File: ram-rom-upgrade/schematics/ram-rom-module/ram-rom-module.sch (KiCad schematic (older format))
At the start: 15 parts, among them SW1 SW_DIP_x08, SW2 SW_Push, U1 74LS245, U2 UM61512A, U3 74LS157, U4 28C256, U5 74LS157, U6 74LS157, U7 74LS00

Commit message: first draft of complete design
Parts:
- BAR1: symbol ram-rom-module-parts:BarGraphLED_8P -> ram-rom-upgrade-symbols:BarGraphLED_8P
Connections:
- net BUS_0: now also U1.18 (B0); no longer U1.11 (B7)
- net BUS_1: now also U1.17 (B1); no longer U1.12 (B6)
- net BUS_2: now also U1.16 (B2); no longer U1.13 (B5)
- net BUS_3: now also U1.15 (B3); no longer U1.14 (B4)
- net BUS_4: now also U1.14 (B4); no longer U1.15 (B3)
- net BUS_5: now also U1.13 (B5); no longer U1.16 (B2)
- net BUS_6: now also U1.12 (B6); no longer U1.17 (B1)
- net BUS_7: now also U1.11 (B7); no longer U1.18 (B0)
- net at BAR1.8 (A), U2.13 (I/O1), U3.4 (Za)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: now also U1.2 (A0); no longer U1.9 (A7)
- net at BAR1.7 (A), U2.14 (I/O2), U3.7 (Zb)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: now also U1.3 (A1); no longer U1.8 (A6)
- net at BAR1.6 (A), U2.15 (I/O3), U3.9 (Zc)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: now also U1.4 (A2); no longer U1.7 (A5)
- net at BAR1.5 (A), U2.17 (I/O4), U3.12 (Zd)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: now also U1.5 (A3); no longer U1.6 (A4)
- net at BAR1.4 (A), U2.18 (I/05), U4.16 (D4)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: now also U1.6 (A4); no longer U1.5 (A3)
- net at BAR1.3 (A), U2.19 (I/O6), U4.17 (D5)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: now also U1.7 (A5); no longer U1.4 (A2)
- net at BAR1.2 (A), U2.20 (I/O7), U4.18 (D6)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: now also U1.8 (A6); no longer U1.3 (A1)
- net at BAR1.1 (A), U2.21 (I/O8), U4.19 (D7)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: now also U1.9 (A7); no longer U1.2 (A0)
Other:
- moved on the sheet: U1, U3
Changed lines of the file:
@@
 	4150 2650 4150 3050
 Wire Wire Line
-	5075 3575 3450 3575
+	5275 3575 3450 3575
 Connection ~ 3450 3575
 Wire Wire Line
-	5375 3500 3550 3500
+	5575 3500 3550 3500
 Connection ~ 3550 3500
-Wire Wire Line
-	5675 3425 3650 3425
 Connection ~ 3650 3425
 Wire Wire Line
-	5975 3350 3750 3350
+	6175 3350 3750 3350
 Connection ~ 3750 3350
 Wire Wire Line
@@
 Connection ~ 4150 3050
 $Comp
-L ram-rom-module-parts:BarGraphLED_8P BAR1
+L ram-rom-upgrade-symbols:BarGraphLED_8P BAR1
 U 1 1 605ABF74
 P 1800 4125
@@
 Wire Wire Line
 	4675 5300 7300 5300
-Wire Wire Line
-	5975 5250 5975 5100
-Wire Wire Line
-	4775 5250 5975 5250
-Wire Wire Line
-	5675 5200 5675 5100
-Wire Wire Line
-	4875 5200 5675 5200
-Wire Wire Line
-	5375 5150 5375 5100
-Wire Wire Line
-	4975 5150 5375 5150
-Connection ~ 5175 6150
+Connection ~ 5375 6150
 Wire Wire Line
 	3450 6150 3450 5100
 Wire Wire Line
-	5175 6150 3450 6150
-Connection ~ 5475 6075
+	5375 6150 3450 6150
+Connection ~ 5675 6075
 Wire Wire Line
 	3550 6075 3550 5100
 Wire Wire Line
-	5475 6075 3550 6075
-Connection ~ 5775 6000
+	5675 6075 3550 6075
+Connection ~ 5975 6000
 Wire Wire Line
 	3650 6000 3650 5100
 Wire Wire Line
-	5775 6000 3650 6000
-Connection ~ 6075 5925
+	5975 6000 3650 6000
+Connection ~ 6275 5925
 Wire Wire Line
 	3750 5925 3750 5100
 Wire Wire Line
-	6075 5925 3750 5925
+	6275 5925 3750 5925
 Connection ~ 7400 5850
 Wire Wire Line
@@
 	8300 5625 4150 5625
 Wire Wire Line
-	5175 6150 5175 5100
-Wire Wire Line
-	8775 6150 5175 6150
-Wire Wire Line
-	5475 6075 5475 5100
-Wire Wire Line
-	8775 6075 5475 6075
-Wire Wire Line
-	5775 6000 5775 5100
-Wire Wire Line
-	8775 6000 5775 6000
-Wire Wire Line
-	6075 5925 6075 5100
-Wire Wire Line
-	8775 5925 6075 5925
+	8775 6150 5375 6150
+Wire Wire Line
+	5675 6075 5675 5100
+Wire Wire Line
+	8775 6075 5675 6075
+Wire Wire Line
+	5975 6000 5975 5100
+Wire Wire Line
+	8775 6000 5975 6000
+Wire Wire Line
+	6275 5925 6275 5100
+Wire Wire Line
+	8775 5925 6275 5925
 Wire Wire Line
 	7400 5850 7400 5100
@@
 L 74xx:74LS245 U1
 U 1 1 60575E88
-P 3650 4600
-F 0 "U1" V 3725 3850 50  0000 L CNN
-F 1 "74LS245" V 3750 4450 50  0000 L CNN
-F 2 "" H 3650 4600 50  0001 C CNN
-F 3 "http://www.ti.com/lit/gpn/sn74LS245" H 3650 4600 50  0001 C CNN
-	1    3650 4600
-	0    1    1    0
+P 3950 4600
+F 0 "U1" V 3700 3850 50  0000 L CNN
+F 1 "74LS245" V 4050 4450 50  0000 L CNN
+F 2 "" H 3950 4600 50  0001 C CNN
+F 3 "http://www.ti.com/lit/gpn/sn74LS245" H 3950 4600 50  0001 C CNN
+	1    3950 4600
+	0    -1   1    0
 $EndComp
 Text HLabel 8775 6150 2    50   BiDi ~ 0
@@
 U 1 1 60556B06
 P 7900 4600
-F 0 "U5" V 7825 5450 50  0000 R CNN
+F 0 "U5" V 8150 3775 50  0000 R CNN
 F 1 "74LS157" V 7925 4725 50  0000 R CNN
 F 2 "" H 7900 4600 50  0001 C CNN
@@
 	0    -1   -1   0
 $EndComp
-$Comp
-L 74xx:74LS157 U3
-U 1 1 6055348B
-P 5675 4600
-F 0 "U3" V 5600 5450 50  0000 R CNN
-F 1 "74LS157" V 5675 4725 50  0000 R CNN
-F 2 "" H 5675 4600 50  0001 C CNN
-F 3 "http://www.ti.com/lit/gpn/sn74LS157" H 5675 4600 50  0001 C CNN
-	1    5675 4600
-	0    -1   -1   0
-$EndComp
 Wire Wire Line
 	8200 3050 8200 4100
@@
 	7300 3275 7300 4100
 Wire Wire Line
-	5975 3350 5975 4100
-Wire Wire Line
-	5675 3425 5675 4100
-Wire Wire Line
-	5375 3500 5375 4100
-Wire Wire Line
-	5075 3575 5075 4100
+	6175 3350 6175 4100
+Wire Wire Line
+	5575 3500 5575 4100
+Wire Wire Line
+	5275 3575 5275 4100
 Wire Wire Line
 	4150 3050 4150 4100
@@
 	4975 700  4975 1725
 Wire Wire Line
-	6375 5100 6675 5100
-Wire Wire Line
-	6675 5100 6675 4600
+	6875 5100 6875 4600
 $Comp
 L power:GND #PWR0104
 U 1 1 608E68AE
-P 6675 5100
-F 0 "#PWR0104" H 6675 4850 50  0001 C CNN
-F 1 "GND" H 6680 4927 50  0000 C CNN
-F 2 "" H 6675 5100 50  0001 C CNN
-F 3 "" H 6675 5100 50  0001 C CNN
-	1    6675 5100
-	1    0    0    -1
-$EndComp
-Connection ~ 6675 5100
+P 6875 5100
+F 0 "#PWR0104" H 6875 4850 50  0001 C CNN
+F 1 "GND" H 6880 4927 50  0000 C CNN
+F 2 "" H 6875 5100 50  0001 C CNN
+F 3 "" H 6875 5100 50  0001 C CNN
+	1    6875 5100
+	1    0    0    -1
+$EndComp
 Wire Wire Line
 	8600 5100 8900 5100
@@
 $EndComp
 Wire Wire Line
-	6275 5100 6275 5500
-Wire Wire Line
-	6275 5500 8500 5500
-Wire Wire Line
 	9200 5500 9200 2675
 Wire Wire Line
 	8500 5100 8500 5500
-Connection ~ 8500 5500
 Wire Wire Line
 	8500 5500 9200 5500
@@
 	6700 2575 6700 3350
 Wire Wire Line
-	6700 3350 5975 3350
-Connection ~ 5975 3350
+	6700 3350 6175 3350
+Connection ~ 6175 3350
 Wire Wire Line
 	6800 2575 6800 3425
 Wire Wire Line
-	6800 3425 5675 3425
-Connection ~ 5675 3425
-Wire Wire Line
 	6900 2575 6900 3500
 Wire Wire Line
-	6900 3500 5375 3500
-Connection ~ 5375 3500
+	6900 3500 5575 3500
+Connection ~ 5575 3500
 Wire Wire Line
 	7000 2575 7000 3575
 Wire Wire Line
-	7000 3575 5075 3575
-Connection ~ 5075 3575
+	7000 3575 5275 3575
+Connection ~ 5275 3575
 Wire Wire Line
 	9200 5500 10500 5500
@@
 L power:VCC #PWR0109
 U 1 1 60C15423
-P 4450 4025
-F 0 "#PWR0109" H 4450 3875 50  0001 C CNN
-F 1 "VCC" H 4465 4198 50  0000 C CNN
-F 2 "" H 4450 4025 50  0001 C CNN
-F 3 "" H 4450 4025 50  0001 C CNN
-	1    4450 4025
-	1    0    0    -1
-$EndComp
-Wire Wire Line
-	3250 4100 3250 4025
-Wire Wire Line
-	3250 4025 4450 4025
-Wire Wire Line
-	4450 4600 4450 4025
-Connection ~ 4450 4025
-Wire Wire Line
-	4775 4600 4775 4025
-Wire Wire Line
-	4775 4025 4450 4025
-Wire Wire Line
-	4775 4025 7000 4025
+P 4975 4025
+F 0 "#PWR0109" H 4975 3875 50  0001 C CNN
+F 1 "VCC" H 4990 4198 50  0000 C CNN
+F 2 "" H 4975 4025 50  0001 C CNN
+F 3 "" H 4975 4025 50  0001 C CNN
+	1    4975 4025
+	1    0    0    -1
+$EndComp
 Wire Wire Line
 	7000 4025 7000 4600
-Connection ~ 4775 4025
+Connection ~ 4975 4025
 Wire Wire Line
 	4375 6925 4375 7000
@@
 	8900 800  8900 825
 Wire Wire Line
-	3150 4100 3150 3650
-Wire Wire Line
-	3150 3650 8900 3650
+	4450 4100 4450 3650
+Wire Wire Line
+	4450 3650 8900 3650
 Wire Wire Line
 	8900 3650 8900 3350
@@
 L power:GND #PWR0113
 U 1 1 60F70DD4
-P 2800 4875
-F 0 "#PWR0113" H 2800 4625 50  0001 C CNN
-F 1 "GND" H 2805 4702 50  0000 C CNN
-F 2 "" H 2800 4875 50  0001 C CNN
-F 3 "" H 2800 4875 50  0001 C CNN
-	1    2800 4875
-	1    0    0    -1
-$EndComp
-Wire Wire Line
-	2850 4600 2800 4600
-Wire Wire Line
-	2800 4600 2800 4875
+P 4750 4600
+F 0 "#PWR0113" H 4750 4350 50  0001 C CNN
+F 1 "GND" H 4755 4427 50  0000 C CNN
+F 2 "" H 4750 4600 50  0001 C CNN
+F 3 "" H 4750 4600 50  0001 C CNN
+	1    4750 4600
+	1    0    0    -1
+$EndComp
 $Comp
 L power:GND #PWR0114
@@
 Wire Wire Line
 	1725 2175 1725 2400
+Wire Wire Line
+	4350 4025 4350 4100
+Wire Wire Line
+	4350 4025 4975 4025
+Connection ~ 5875 3425
+Wire Wire Line
+	6800 3425 5875 3425
+Wire Wire Line
+	5875 3425 3650 3425
+Wire Wire Line
+	5875 3425 5875 4100
+$Comp
+L 74xx:74LS157 U3
+U 1 1 6055348B
+P 5875 4600
+F 0 "U3" V 6125 3775 50  0000 R CNN
+F 1 "74LS157" V 5875 4775 50  0000 R CNN
+F 2 "" H 5875 4600 50  0001 C CNN
+F 3 "http://www.ti.com/lit/gpn/sn74LS157" H 5875 4600 50  0001 C CNN
+	1    5875 4600
+	0    -1   -1   0
+$EndComp
+Wire Wire Line
+	8500 5500 6475 5500
+Wire Wire Line
+	6475 5500 6475 5100
+Connection ~ 8500 5500
+Wire Wire Line
+	6575 5100 6875 5100
+Connection ~ 6875 5100
+Wire Wire Line
+	6175 5250 6175 5100
+Wire Wire Line
+	4775 5250 6175 5250
+Wire Wire Line
+	5375 5100 5375 6150
+Wire Wire Line
+	5075 5100 5275 5100
+Wire Wire Line
+	4975 5150 5575 5150
+Wire Wire Line
+	5575 5150 5575 5100
+Wire Wire Line
+	4875 5200 5875 5200
+Wire Wire Line
+	5875 5200 5875 5100
+Wire Wire Line
+	4975 4600 4975 4025
+Wire Wire Line
+	4975 4025 7000 4025
+Wire Wire Line
+	3150 4600 3150 4025
+Wire Wire Line
+	3150 4025 4350 4025
+Connection ~ 4350 4025
 $EndSCHEMATC

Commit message: fixed bus contention issue
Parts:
- added unit 3 of U7
- added U8: 74LS32, symbol 74xx:74LS32
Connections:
- net GND: no longer U2.24 (~OE), U3.15 (E), U4.22 (~OE), U5.15 (E)
- net RMi: now also U7.2, U8.2; no longer U7.5
- net at U6.13 (I1d): now also U7.6; no longer U7.3
- net at R2.2, SW2.1, U6.14 (I0d): now also U8.1
- net at C1.2, R1.1: now also U7.1; no longer U7.4
- new net: U2.24 (~OE), U4.22 (~OE), U7.10, U7.9, U8.3
- new net: U3.15 (E), U5.15 (E), U7.8
- new net: U7.3, U7.4, U7.5
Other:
- note added: "NOTE: This OR gate prevents the ROM & RAM \nfrom outputing to the bus if the 74LS157s are\nactive. The 74LS157s are active is RMi or the \nmanual memory write buttons are high."
- moved on the sheet: BAR1, C1, D1, R1, R2, RN1, SW1, SW2, U1, U2, U3, U4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

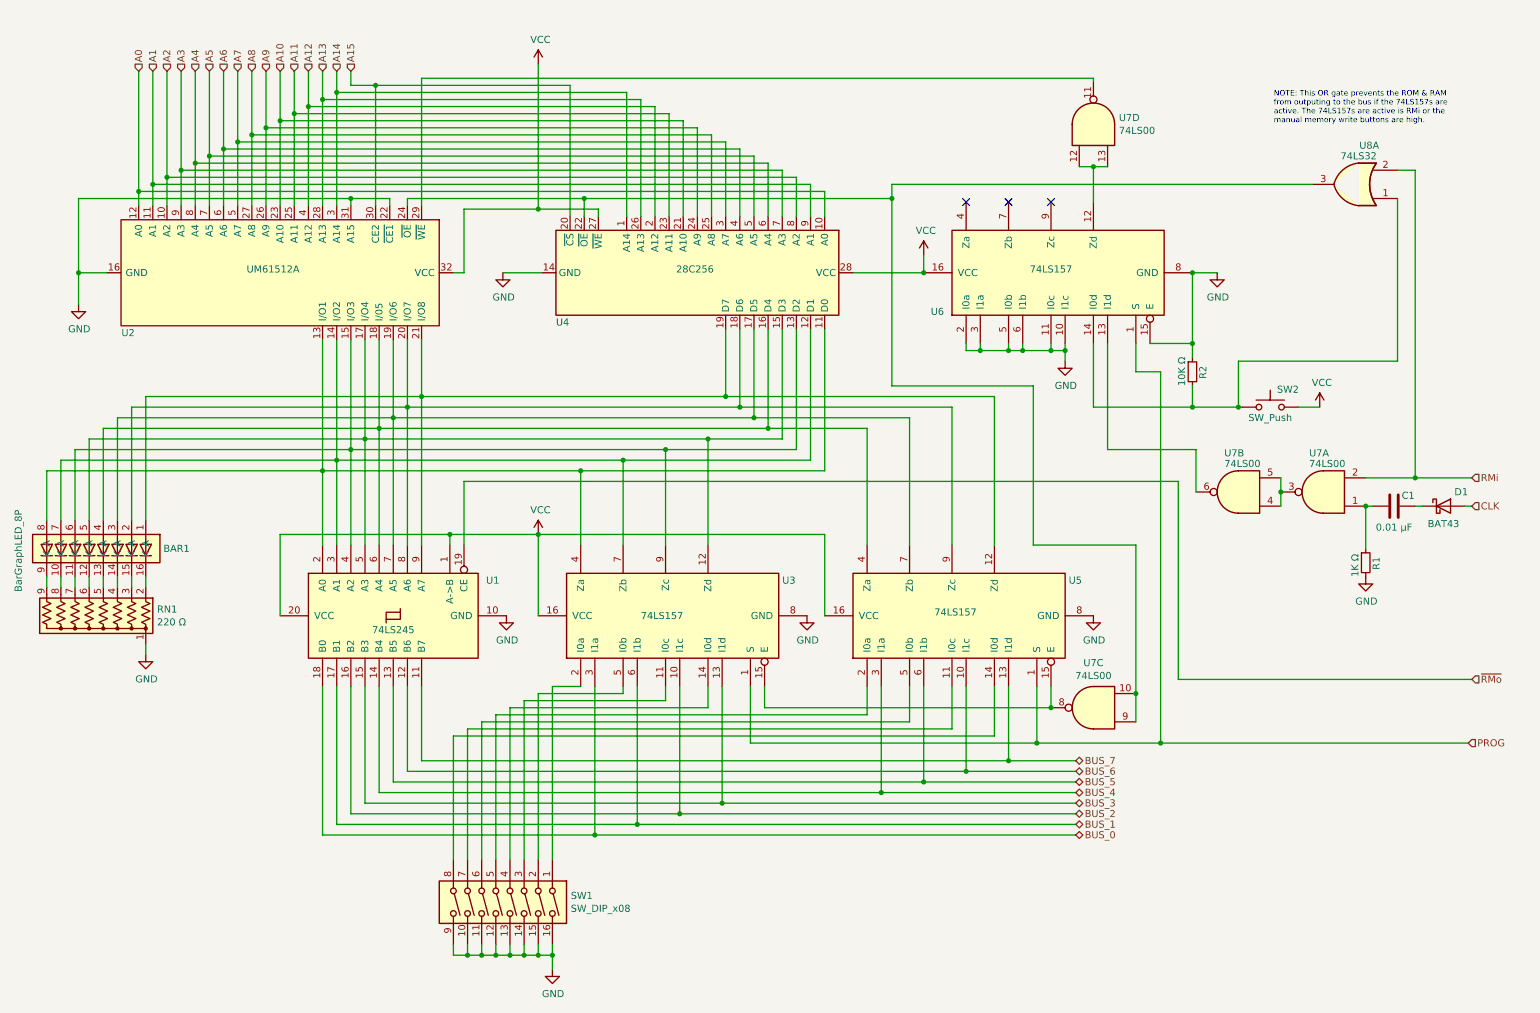
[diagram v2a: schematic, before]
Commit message: further fixed bus contention issue
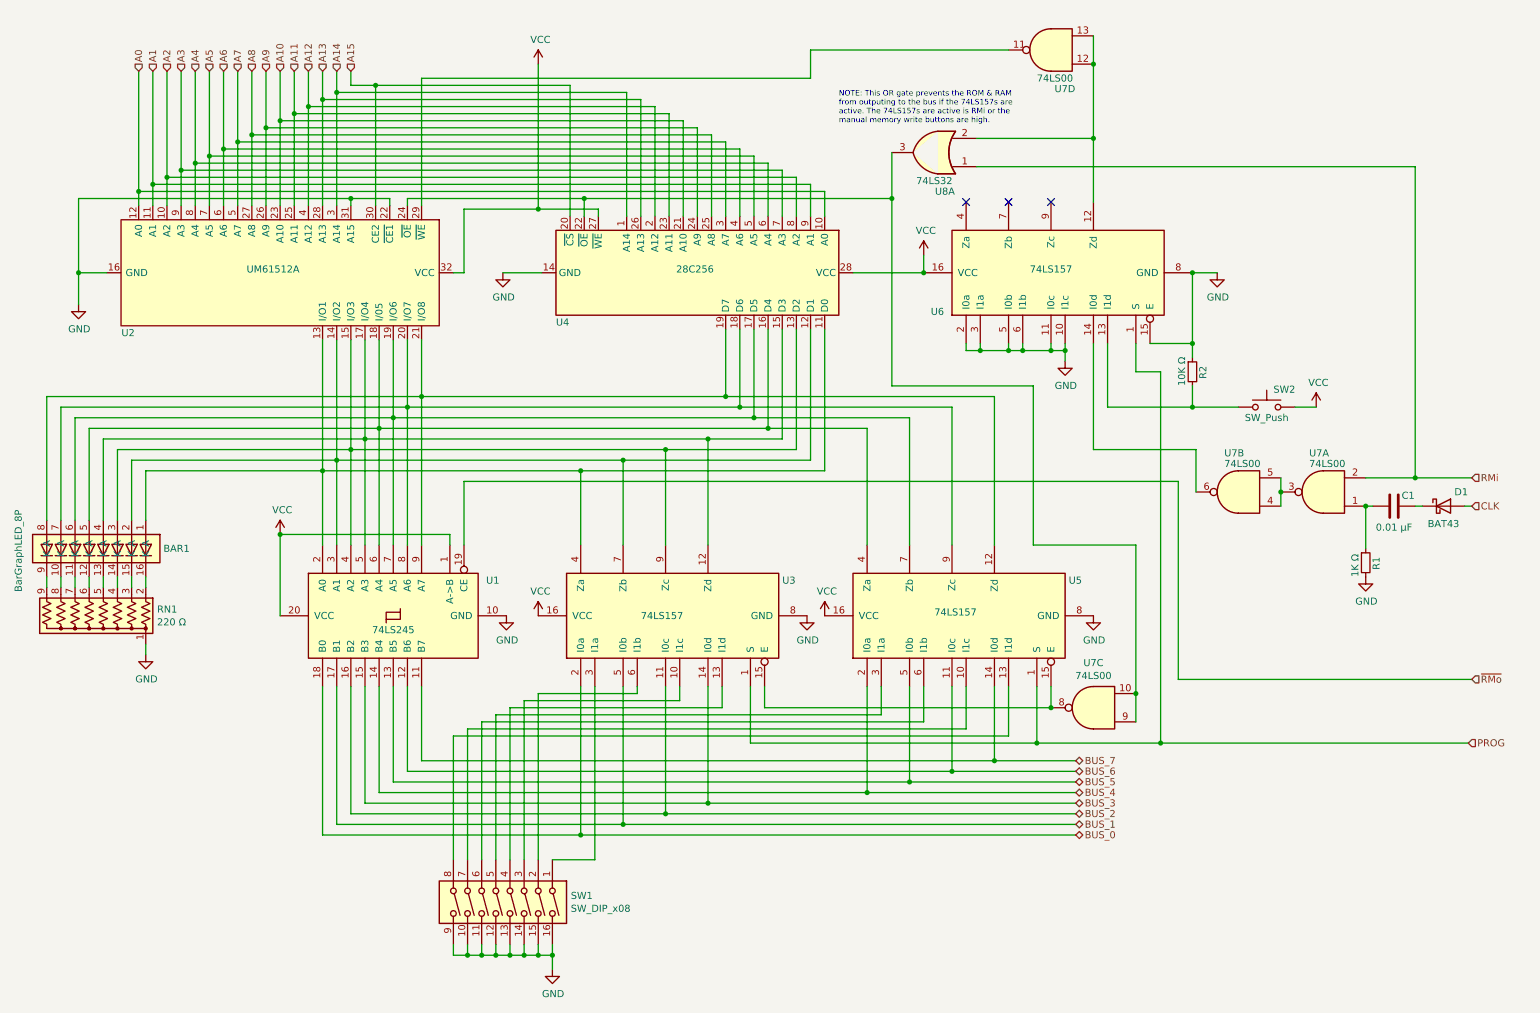
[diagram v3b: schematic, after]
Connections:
- net BUS_0: now also U3.2 (I0a); no longer U3.3 (I1a)
- net BUS_1: now also U3.5 (I0b); no longer U3.6 (I1b)
- net BUS_2: now also U3.11 (I0c); no longer U3.10 (I1c)
- net BUS_3: now also U3.14 (I0d); no longer U3.13 (I1d)
- net BUS_4: now also U5.2 (I0a); no longer U5.3 (I1a)
- net BUS_5: now also U5.5 (I0b); no longer U5.6 (I1b)
- net BUS_6: now also U5.11 (I0c); no longer U5.10 (I1c)
- net BUS_7: now also U5.14 (I0d); no longer U5.13 (I1d)
- net RMi: now also U8.1; no longer U8.2
- net at U1.2 (A0), U2.13 (I/O1), U3.4 (Za)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: now also BAR1.1 (A); no longer BAR1.8 (A)
- net at U1.3 (A1), U2.14 (I/O2), U3.7 (Zb)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: now also BAR1.2 (A); no longer BAR1.7 (A)
- net at U1.4 (A2), U2.15 (I/O3), U3.9 (Zc)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: now also BAR1.3 (A); no longer BAR1.6 (A)
- net at U1.5 (A3), U2.17 (I/O4), U3.12 (Zd)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: now also BAR1.4 (A); no longer BAR1.5 (A)
- net at U1.6 (A4), U2.18 (I/05), U4.16 (D4)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: now also BAR1.5 (A); no longer BAR1.4 (A)
- net at U1.7 (A5), U2.19 (I/O6), U4.17 (D5)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: now also BAR1.6 (A); no longer BAR1.3 (A)
- net at U1.8 (A6), U2.20 (I/O7), U4.18 (D6)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: now also BAR1.7 (A); no longer BAR1.2 (A)
- net at U1.9 (A7), U2.21 (I/O8), U4.19 (D7)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: now also BAR1.8 (A); no longer BAR1.1 (A)
- net at SW1.3: now also U3.10 (I1c); no longer U3.11 (I0c)
- net at SW1.4: now also U3.13 (I1d); no longer U3.14 (I0d)
- net at SW1.1: now also U3.3 (I1a); no longer U3.2 (I0a)
- net at SW1.2: now also U3.6 (I1b); no longer U3.5 (I0b)
- net at SW1.7: now also U5.10 (I1c); no longer U5.11 (I0c)
- net at SW1.8: now also U5.13 (I1d); no longer U5.14 (I0d)
- net at SW1.5: now also U5.3 (I1a); no longer U5.2 (I0a)
- net at SW1.6: now also U5.6 (I1b); no longer U5.5 (I0b)
- net at R2.2, SW2.1: now also U6.13 (I1d); no longer U6.14 (I0d), U8.1
- net at U6.12 (Zd), U7.12, U7.13: now also U8.2
- net at U7.6: now also U6.14 (I0d); no longer U6.13 (I1d)
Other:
- moved on the sheet: SW2, U7D, U8A
